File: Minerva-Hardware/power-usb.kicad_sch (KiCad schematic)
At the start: 48 parts, among them J24 BATT JST-PH 2P, U1 BQ25798, U30 TPS61088RHLR, U31 MAX17048G+T10

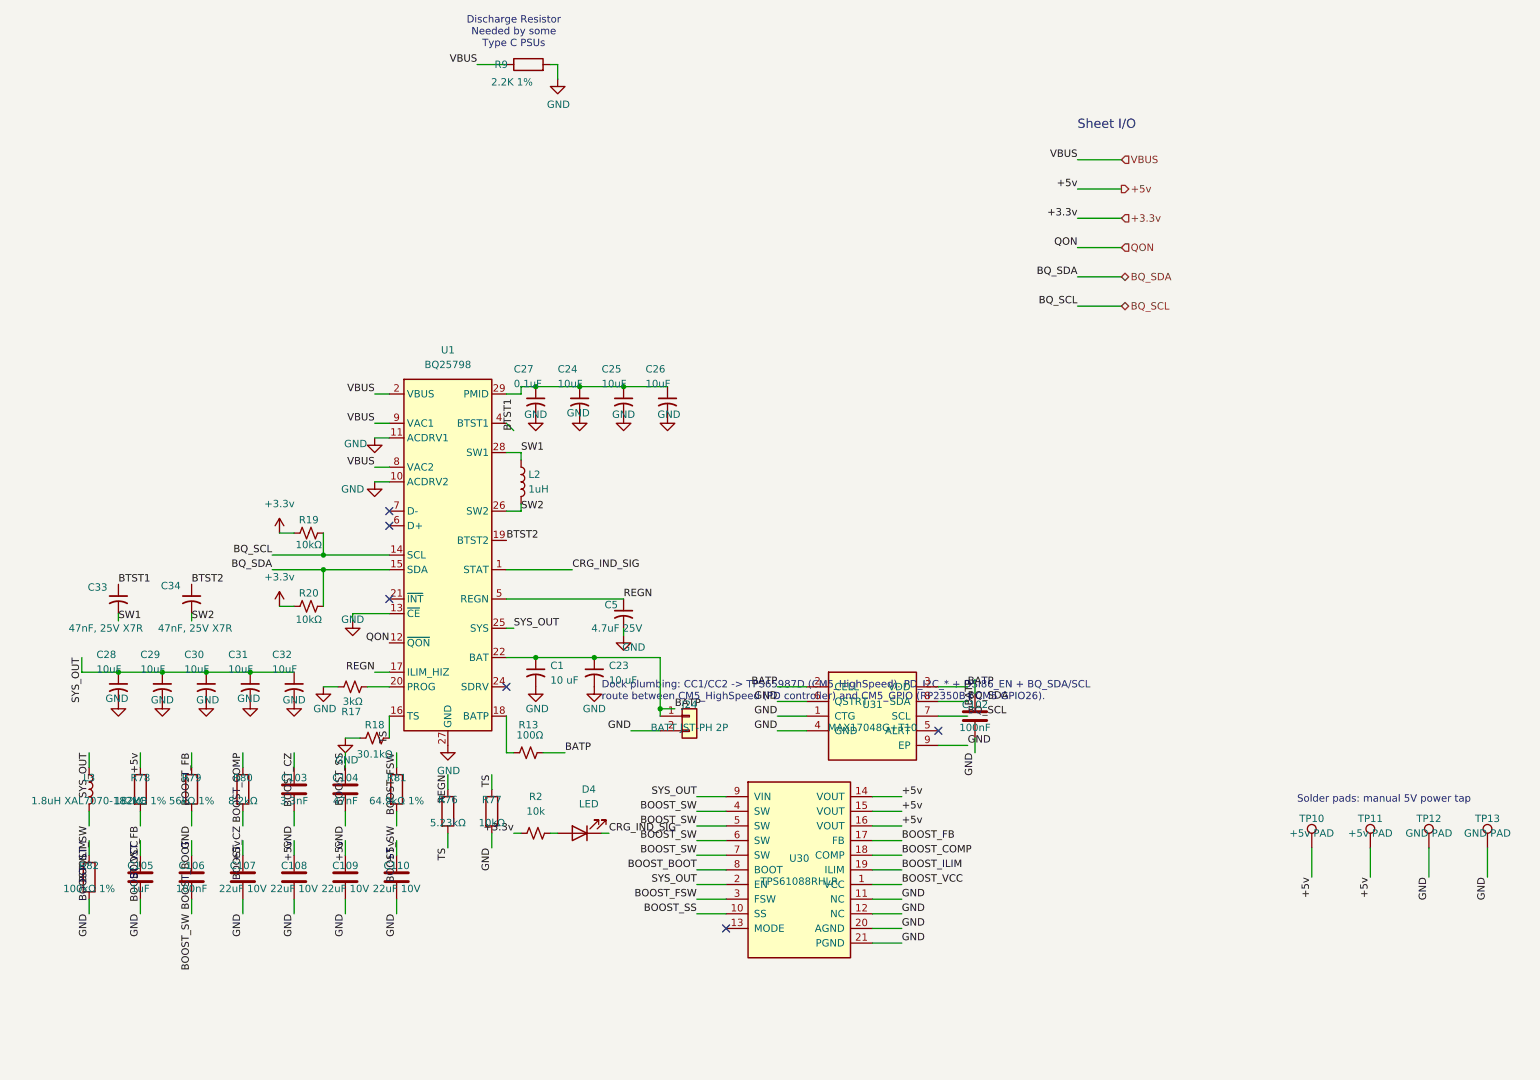
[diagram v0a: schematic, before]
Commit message: hardware: snapshot carrier and face-board integration
Hardware schematics and power:
- complete the BQ25798 charger, TPS61088 5 V boost, MAX17048 gauge, battery controls, and cross-sheet power hierarchy
- add the SN65DSI86 display bridge, HD3SS460 mux, TPS65987D PD controller, USB-C protection, M.2 support, and corrected named-interface wiring
- move the Core2350B0 onto the face-board interconnect, route controls through J25/J2, and make Select directly assert nRPIBOOT
- remove the obsolete J6/J8 expansion headers and move J23 USB-C to the carrier top-left with its VBUS switch and charger support cluster

PCB, footprints, and mechanical assets:
- establish the six-layer controlled-impedance carrier stack, net classes, HDI rules, ground/power planes, keepouts, and placed carrier floorplan
- add the routed two-layer Minerva-Face board with eleven controls, four M2.5 holes, interconnects, fiducials, and a 3.5-inch display datum
- add corrected project-local footprints and STEP models for Core2350B0, USB-C, bridge/PD/power ICs, PicoBlade connectors, M.2 hardware, and critical mechanical envelopes
- correct BAT54 pin mapping, TPS61088 thermal-via numbering, J23 shell geometry, and board-edge lug rules

Verification and reference material:
- add sourcing evidence, ERC/DRC artifacts, STEP assemblies, face render, mechanical coordinates, controlled-impedance notes, and strict connectivity checklists
- document the dock architecture and current board-to-board pin contract
- remove transient root-level DRC and netlist dumps

Torchform and workstation integration:
- fix four-column home navigation and add controller focus/adjustment for quick-settings volume and brightness sliders
- configure Kitty as the terminal backend and add the Minerva SSH workspace folder

Known work-in-progress at this snapshot:
- carrier schematic/PCB parity is clean, but routing remains incomplete at 499 unconnected items with 53 differential-pair tuning violations
- the face board is DRC-clean and f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
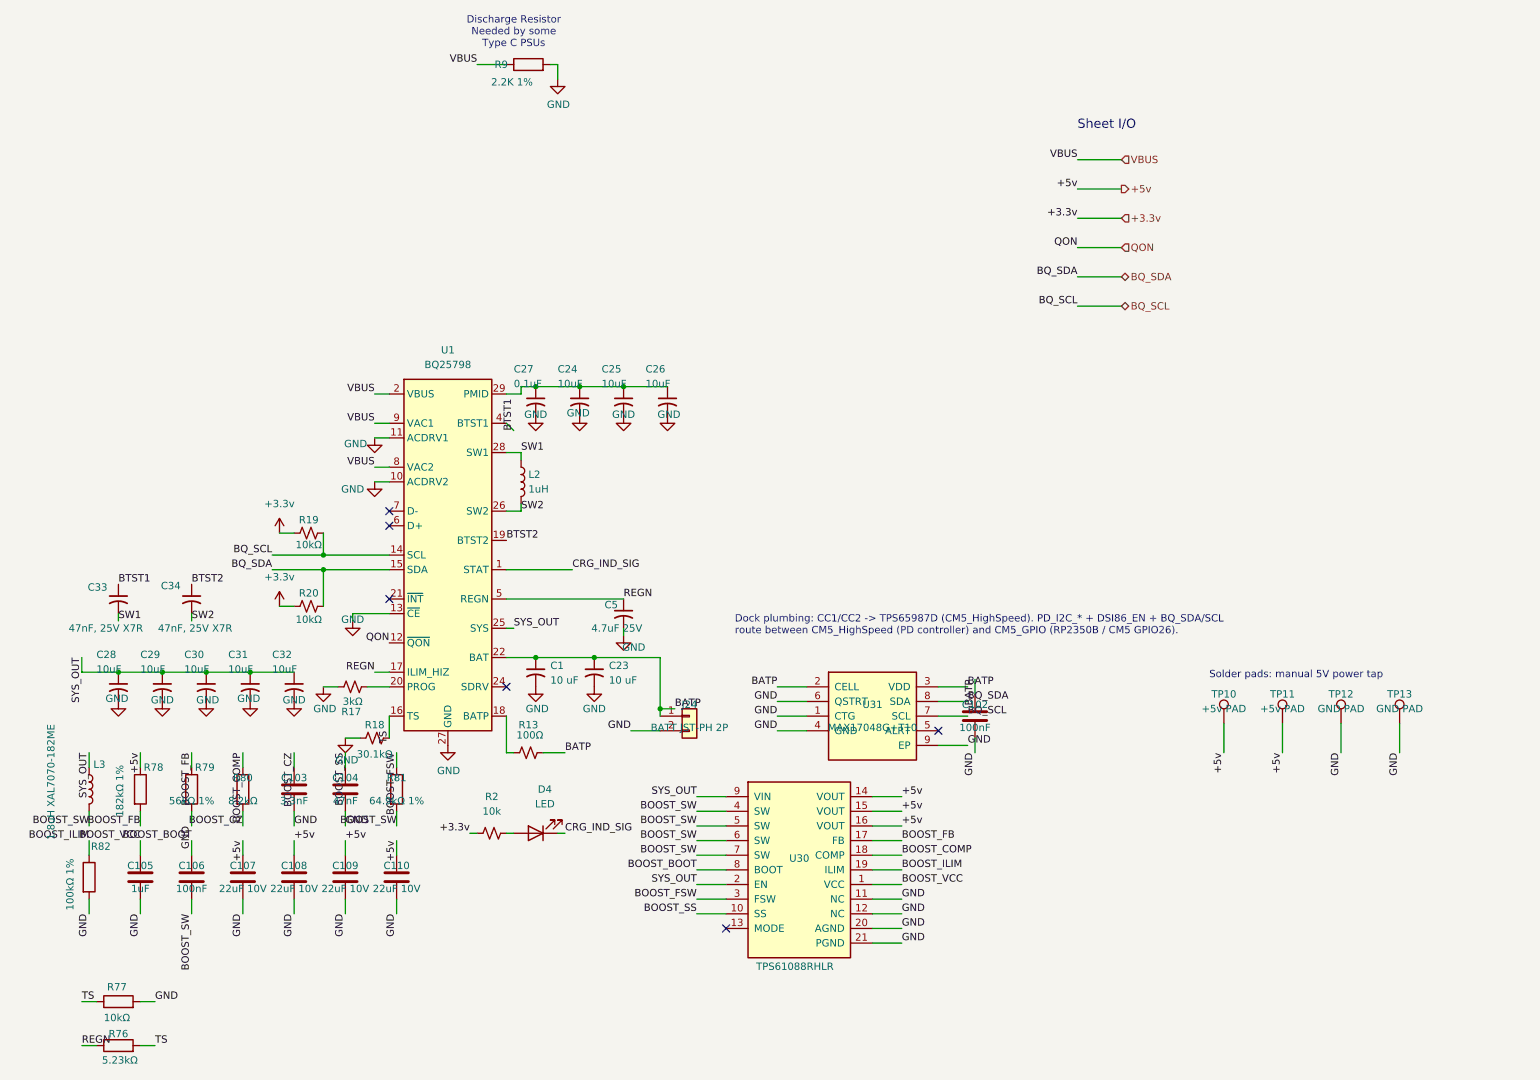
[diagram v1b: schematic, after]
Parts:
- C1, C23: footprint Capacitor_SMD:C_0201_0603Metric -> Capacitor_SMD:C_0603_1608Metric; MPN (none) -> CL10A106KP8NNNC; Manufacturer (none) -> Samsung Electro-Mechanics
- C102, C106: MPN (none) -> EMK105B7104KV-F; Manufacturer (none) -> Taiyo Yuden
- C103: MPN (none) -> GRM1555C1H332JE01D; Manufacturer (none) -> Murata
- C104: MPN (none) -> GRM155R71E473KA88D; Manufacturer (none) -> Murata
- C105: MPN (none) -> CC0402KRX5R6BB105; Manufacturer (none) -> Yageo
- C107, C108, C109, C110: MPN (none) -> GRM21BR61A226ME44L; Manufacturer (none) -> Murata
- C24, C25, C26: footprint Capacitor_SMD:C_01005_0402Metric -> Capacitor_SMD:C_0805_2012Metric; MPN (none) -> GRM21BR61E106KA73L; Manufacturer (none) -> Murata
- C27: footprint Capacitor_SMD:C_01005_0402Metric -> Capacitor_SMD:C_0402_1005Metric; MPN (none) -> GRM155R71H104KE14D; Manufacturer (none) -> Murata
- C28, C29, C30, C31, C32: footprint Capacitor_SMD:C_01005_0402Metric -> Capacitor_SMD:C_0603_1608Metric; MPN (none) -> CL10A106KP8NNNC; Manufacturer (none) -> Samsung Electro-Mechanics
- C33, C34: footprint Capacitor_SMD:C_01005_0402Metric -> Capacitor_SMD:C_0402_1005Metric; MPN (none) -> GRM155R71E473KA88D; Manufacturer (none) -> Murata
- C5: footprint Capacitor_SMD:C_0201_0603Metric -> Capacitor_SMD:C_0603_1608Metric; MPN (none) -> GRM188R61E475KE11D; Manufacturer (none) -> Murata
- D4: footprint LED_SMD:LED_0201_0603Metric -> LED_SMD:LED_0402_1005Metric; MPN (none) -> SML-P12UTT86R; Manufacturer (none) -> ROHM
- J24: MPN (none) -> B2B-PH-K-S(LF)(SN); Manufacturer (none) -> JST
- L2: MPN (none) -> SRP5030T-1R0M; Manufacturer (none) -> Bourns
- L3: MPN (none) -> XAL7070-182MEC; Manufacturer (none) -> Coilcraft
- R13: MPN (none) -> RC0402FR-07100RL; Manufacturer (none) -> Yageo
- R17: MPN (none) -> RC0402FR-073KL; Manufacturer (none) -> Yageo
- R18: MPN (none) -> RC0402FR-0730K1L; Manufacturer (none) -> Yageo
- R19, R20, R77: MPN (none) -> RC0402FR-0710KL; Manufacturer (none) -> Yageo
- R2: footprint Resistor_SMD:R_0201_0603Metric -> Resistor_SMD:R_0402_1005Metric; MPN (none) -> RC0402FR-0710KL; Manufacturer (none) -> Yageo
- R76: MPN (none) -> CRCW04025K23FKED; Manufacturer (none) -> Vishay
- R78: MPN (none) -> RC0402FR-07182KL; Manufacturer (none) -> Yageo
- R79: MPN (none) -> RC0402FR-0756KL; Manufacturer (none) -> Yageo
- R80: MPN (none) -> RT0402FRE078K2L; Manufacturer (none) -> Yageo
- R81: MPN (none) -> CRCW040264K9FKED; Manufacturer (none) -> Vishay
- R82: MPN (none) -> RC0402FR-07100KL; Manufacturer (none) -> Yageo
- R9: MPN (none) -> RT0402FRE072K2L; Manufacturer (none) -> Yageo
- TP10, TP11, TP12, TP13: MPN (none) -> N/A; Manufacturer (none) -> PCB fabrication; Procurement Note (none) -> PCB feature; not purchased or placed; now left out of the parts list
- U1: MPN (none) -> BQ25798RQMR; Manufacturer (none) -> Texas Instruments
- U30: MPN (none) -> TPS61088RHLR; Manufacturer (none) -> Texas Instruments
- U31: MPN (none) -> MAX17048G+T10; Manufacturer (none) -> Analog Devices / Maxim Integrated
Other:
- moved on the sheet: D4, R2, R76, R77, TP10, TP11, TP12, TP13
